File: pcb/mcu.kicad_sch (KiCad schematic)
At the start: 13 parts, among them J2 Conn_02x03_Counter_Clockwise, SW6 SW_MEC_5E, U3 STM32F042K6Tx, U4 TLV70033_SOT23-5

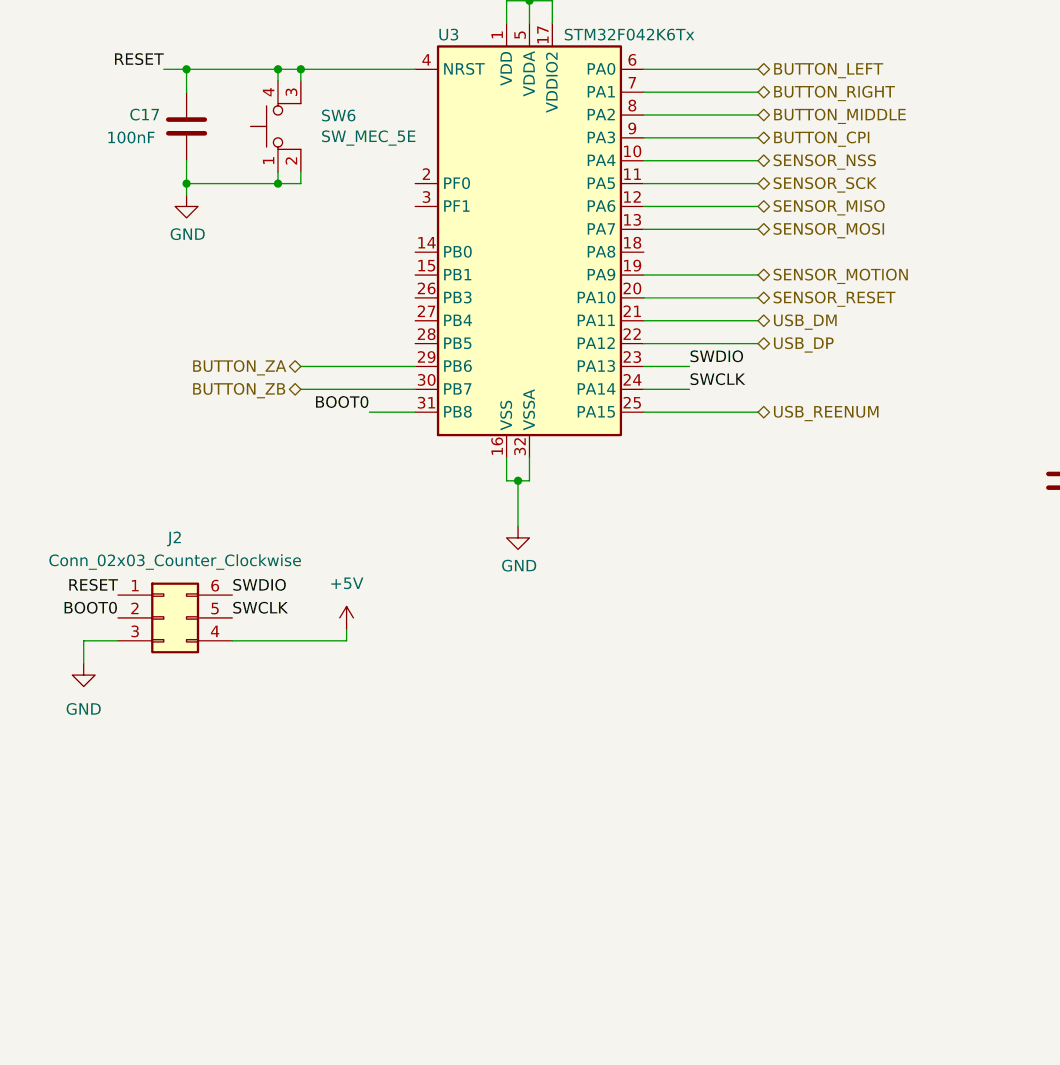
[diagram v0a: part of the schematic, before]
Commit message: - added debouncing to buttons - assigned some footprints - added expansion and inspection pin headers
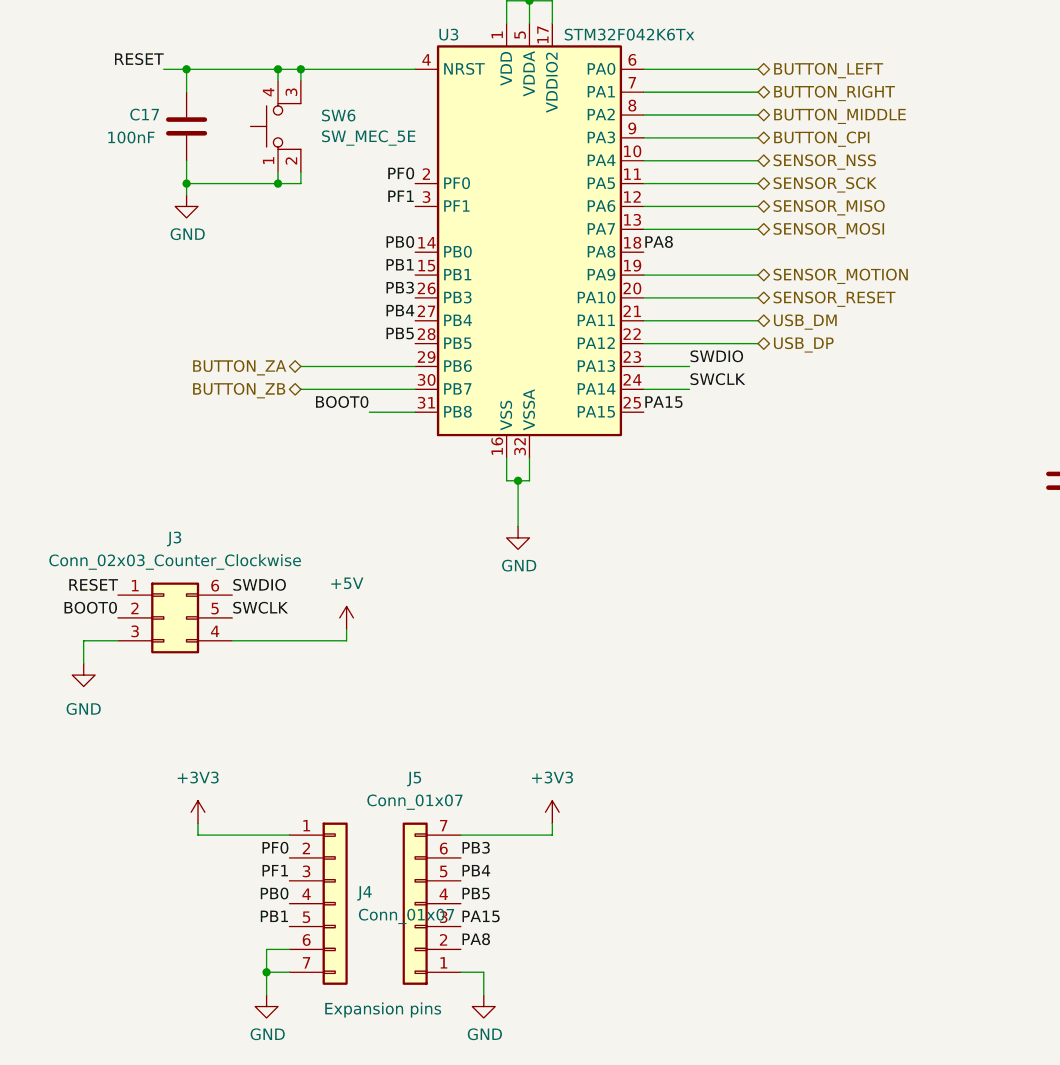
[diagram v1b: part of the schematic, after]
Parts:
- added J4, J5: Conn_01x07, Connector_PinSocket_2.54mm:PinSocket_1x07_P2.54mm_Vertical, symbol Connector_Generic:Conn_01x07
- renumbered J2 to J3
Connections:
- net +3V3: now also J4.1 (Pin_1), J5.7 (Pin_7)
- net GND: now also J4.6 (Pin_6), J4.7 (Pin_7), J5.1 (Pin_1)
- net PB0: now reaches U3.14 (PB0)
- net PB0: now also J4.4 (Pin_4)
- net PB1: now reaches U3.15 (PB1)
- net PB1: now also J4.5 (Pin_5)
- net PA8: now reaches U3.18 (PA8)
- net PA8: now also J5.2 (Pin_2)
- net PF0: now reaches U3.2 (PF0)
- net PF0: now also J4.2 (Pin_2)
- net PB3: now reaches U3.26 (PB3)
- net PB3: now also J5.6 (Pin_6)
- net PB4: now reaches U3.27 (PB4)
- net PB4: now also J5.5 (Pin_5)
- net PB5: now reaches U3.28 (PB5)
- net PB5: now also J5.4 (Pin_4)
- net PF1: now reaches U3.3 (PF1)
- net PF1: now also J4.3 (Pin_3)
- net USB_REENUM renamed PA15
- net PA15: now also J5.3 (Pin_3)
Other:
- note added: "Expansion pins"

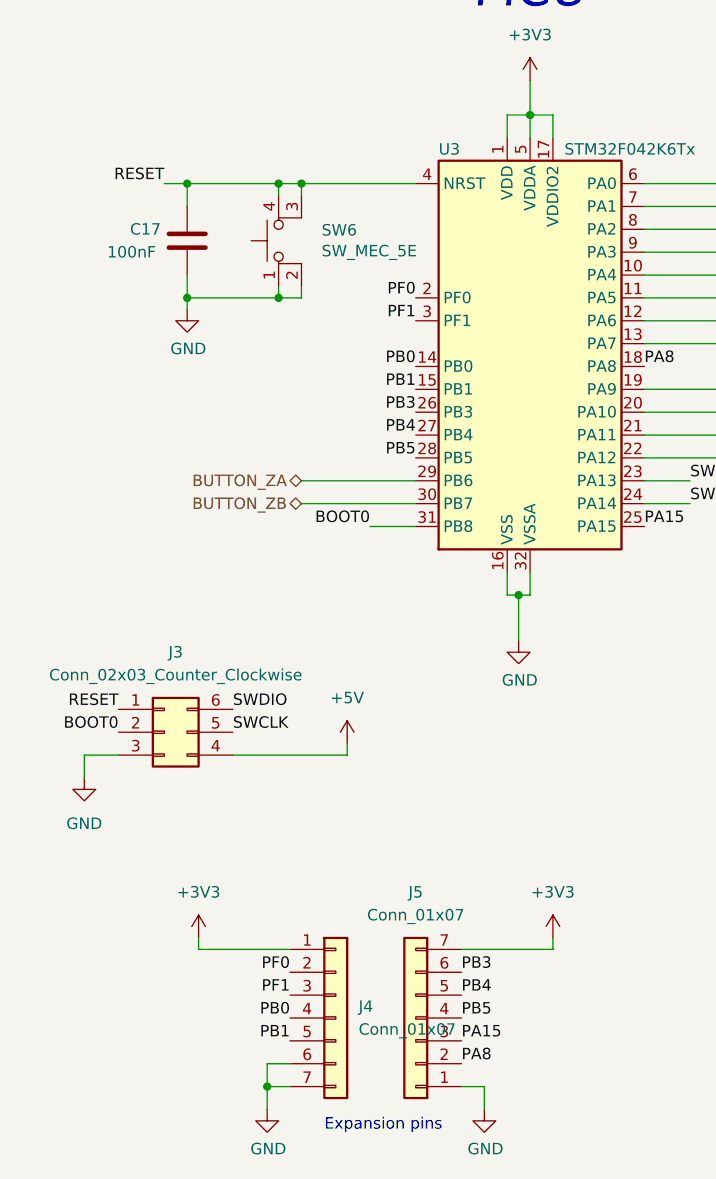
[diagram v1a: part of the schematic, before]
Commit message: - added rotary encoder debouncing - added mouse switch and encoder footprints - changed some symbols - assigned footprints
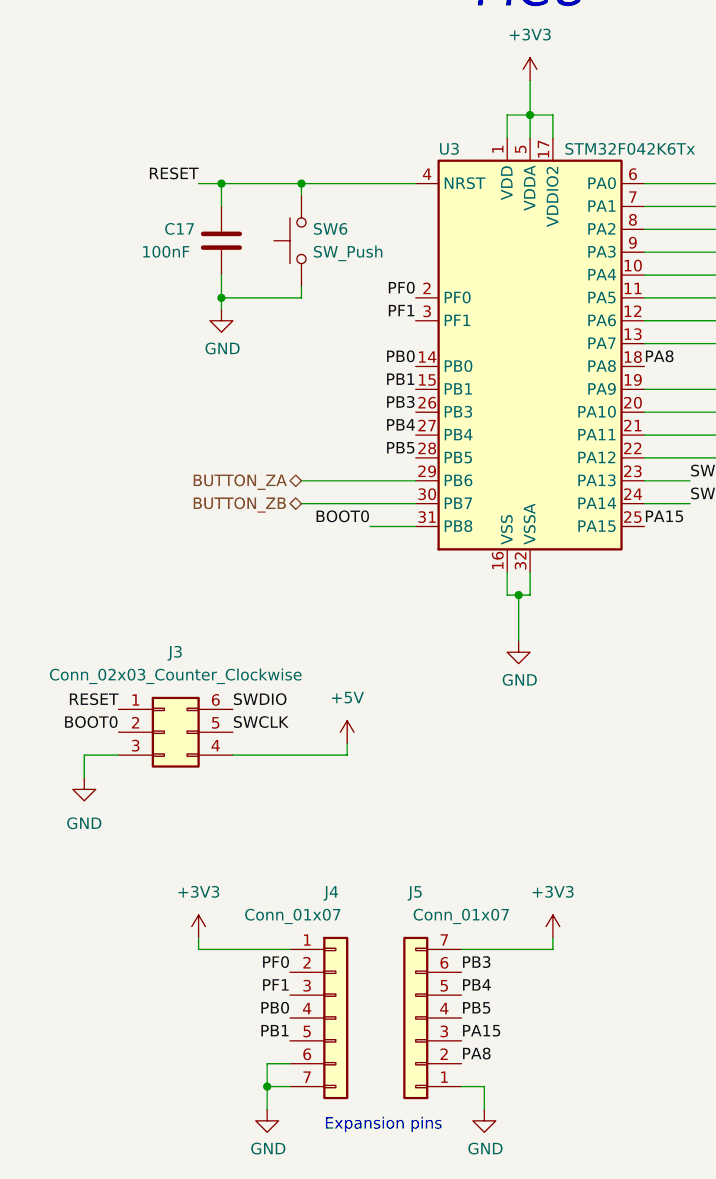
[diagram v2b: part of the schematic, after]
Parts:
- removed SW6: SW_MEC_5E, symbol Switch:SW_MEC_5E
- added SW6: SW_Push, Button_Switch_THT:SW_PUSH_6mm, symbol Switch:SW_Push
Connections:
- net GND: now also SW6.1
- net RESET: now also SW6.2
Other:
- moved on the sheet: C17
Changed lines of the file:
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@@
   (junction (at 233.68 64.77) (diameter 0) (color 0 0 0 0)
   )
-  (junction (at 92.71 76.2) (diameter 0) (color 0 0 0 0)
-  )
-  (junction (at 92.71 63.5) (diameter 0) (color 0 0 0 0)
+  (junction (at 96.52 76.2) (diameter 0) (color 0 0 0 0)
+  )
+  (junction (at 96.52 63.5) (diameter 0) (color 0 0 0 0)
   )
   (junction (at 219.71 114.3) (diameter 0) (color 0 0 0 0)
@@
   (junction (at 105.41 63.5) (diameter 0) (color 0 0 0 0)
   )
-  (junction (at 102.87 76.2) (diameter 0) (color 0 0 0 0)
-  )
   (junction (at 101.6 163.83) (diameter 0) (color 0 0 0 0)
   )
   (junction (at 208.28 64.77) (diameter 0) (color 0 0 0 0)
   )
-  (junction (at 102.87 63.5) (diameter 0) (color 0 0 0 0)
-  )
   (junction (at 219.71 104.14) (diameter 0) (color 0 0 0 0)
   )
@@
     (stroke (width 0) (type default) (color 0 0 0 0))
   )
-  (wire (pts (xy 92.71 66.04) (xy 92.71 63.5))
+  (wire (pts (xy 96.52 66.04) (xy 96.52 63.5))
     (stroke (width 0) (type default) (color 0 0 0 0))
   )
@@
     (stroke (width 0) (type default) (color 0 0 0 0))
   )
-  (wire (pts (xy 102.87 63.5) (xy 102.87 64.77))
-    (stroke (width 0) (type default) (color 0 0 0 0))
-  )
   (wire (pts (xy 214.63 114.3) (xy 219.71 114.3))
     (stroke (width 0) (type default) (color 0 0 0 0))
@@
     (stroke (width 0) (type default) (color 0 0 0 0))
   )
-  (wire (pts (xy 102.87 76.2) (xy 105.41 76.2))
-    (stroke (width 0) (type default) (color 0 0 0 0))
-  )
   (wire (pts (xy 81.28 127) (xy 81.28 129.54))
     (stroke (width 0) (type default) (color 0 0 0 0))
@@
     (stroke (width 0) (type default) (color 0 0 0 0))
   )
-  (wire (pts (xy 105.41 63.5) (xy 102.87 63.5))
-    (stroke (width 0) (type default) (color 0 0 0 0))
-  )
   (wire (pts (xy 219.71 114.3) (xy 226.06 114.3))
     (stroke (width 0) (type default) (color 0 0 0 0))
@@
     (stroke (width 0) (type default) (color 0 0 0 0))
   )
-  (wire (pts (xy 92.71 77.47) (xy 92.71 76.2))
+  (wire (pts (xy 96.52 77.47) (xy 96.52 76.2))
     (stroke (width 0) (type default) (color 0 0 0 0))
   )
@@
     (stroke (width 0) (type default) (color 0 0 0 0))
   )
-  (wire (pts (xy 90.17 63.5) (xy 92.71 63.5))
+  (wire (pts (xy 93.98 63.5) (xy 96.52 63.5))
     (stroke (width 0) (type default) (color 0 0 0 0))
   )
@@
     (stroke (width 0) (type default) (color 0 0 0 0))
   )
-  (wire (pts (xy 102.87 74.93) (xy 102.87 76.2))
-    (stroke (width 0) (type default) (color 0 0 0 0))
-  )
   (wire (pts (xy 130.81 52.07) (xy 130.81 55.88))
     (stroke (width 0) (type default) (color 0 0 0 0))
@@
     (stroke (width 0) (type default) (color 0 0 0 0))
   )
-  (wire (pts (xy 92.71 76.2) (xy 102.87 76.2))
+  (wire (pts (xy 96.52 76.2) (xy 105.41 76.2))
     (stroke (width 0) (type default) (color 0 0 0 0))
   )
@@
     (stroke (width 0) (type default) (color 0 0 0 0))
   )
-  (wire (pts (xy 92.71 63.5) (xy 102.87 63.5))
-    (stroke (width 0) (type default) (color 0 0 0 0))
-  )
-  (wire (pts (xy 92.71 73.66) (xy 92.71 76.2))
+  (wire (pts (xy 96.52 63.5) (xy 105.41 63.5))
+    (stroke (width 0) (type default) (color 0 0 0 0))
+  )
+  (wire (pts (xy 96.52 73.66) (xy 96.52 76.2))
     (stroke (width 0) (type default) (color 0 0 0 0))
   )
@@
     (effects (font (size 1.27 1.27)) (justify left bottom))
   )
-  (label "RESET" (at 90.17 63.5 180)
+  (label "RESET" (at 93.98 63.5 180)
     (effects (font (size 1.27 1.27)) (justify right bottom))
   )
@@
     (pin "1")
     (pin "2")
-  )
-  (symbol (lib_id "Switch:SW_MEC_5E") (at 105.41 69.85 90) (unit 1)
-    (in_bom yes) (on_board yes)
-    (property "Reference" "SW6" (id 0) (at 107.6452 68.6816 90)
-      (effects (font (size 1.27 1.27)) (justify right))
-    )
-    (property "Value" "SW_MEC_5E" (id 1) (at 107.6452 70.993 90)
-      (effects (font (size 1.27 1.27)) (justify right))
-    )
-    (property "Footprint" "" (id 2) (at 97.79 69.85 0)
-      (effects (font (size 1.27 1.27)) hide)
-    )
-    (property "Datasheet" "http://www.apem.com/int/index.php?controller=attachment&id_attachment=1371" (id 3) (at 97.79 69.85 0)
-      (effects (font (size 1.27 1.27)) hide)
-    )
-    (pin "1")
-    (pin "2")
-    (pin "3")
-    (pin "4")
   )
   (symbol (lib_id "power:+3V3") (at 130.81 52.07 0) (unit 1)
@@
     (pin "1")
   )
-  (symbol (lib_id "Device:C") (at 92.71 69.85 0) (unit 1)
-    (in_bom yes) (on_board yes)
-    (property "Reference" "C17" (id 0) (at 86.36 68.58 0)
-      (effects (font (size 1.27 1.27)) (justify left))
-    )
-    (property "Value" "100nF" (id 1) (at 83.82 71.12 0)
-      (effects (font (size 1.27 1.27)) (justify left))
-    )
-    (property "Footprint" "Capacitor_SMD:C_0603_1608Metric" (id 2) (at 93.6752 73.66 0)
-      (effects (font (size 1.27 1.27)) hide)
-    )
-    (property "Datasheet" "~" (id 3) (at 92.71 69.85 0)
+  (symbol (lib_id "Device:C") (at 96.52 69.85 0) (unit 1)
+    (in_bom yes) (on_board yes)
+    (property "Reference" "C17" (id 0) (at 90.17 68.58 0)
+      (effects (font (size 1.27 1.27)) (justify left))
+    )
+    (property "Value" "100nF" (id 1) (at 87.63 71.12 0)
+      (effects (font (size 1.27 1.27)) (justify left))
+    )
+    (property "Footprint" "Capacitor_SMD:C_0603_1608Metric" (id 2) (at 97.4852 73.66 0)
+      (effects (font (size 1.27 1.27)) hide)
+    )
+    (property "Datasheet" "~" (id 3) (at 96.52 69.85 0)
       (effects (font (size 1.27 1.27)) hide)
     )
@@
     (pin "1")
   )
-  (symbol (lib_id "power:GND") (at 92.71 77.47 0) (unit 1)
-    (in_bom yes) (on_board yes)
-    (property "Reference" "#PWR033" (id 0) (at 92.71 83.82 0)
-      (effects (font (size 1.27 1.27)) hide)
-    )
-    (property "Value" "GND" (id 1) (at 92.837 81.8642 0))
-    (property "Footprint" "" (id 2) (at 92.71 77.47 0)
-      (effects (font (size 1.27 1.27)) hide)
-    )
-    (property "Datasheet" "" (id 3) (at 92.71 77.47 0)
+  (symbol (lib_id "Switch:SW_Push") (at 105.41 69.85 90) (unit 1)
+    (in_bom yes) (on_board yes) (fields_autoplaced)
+    (property "Reference" "SW6" (id 0) (at 106.68 68.5799 90)
+      (effects (font (size 1.27 1.27)) (justify right))
+    )
+    (property "Value" "SW_Push" (id 1) (at 106.68 71.1199 90)
+      (effects (font (size 1.27 1.27)) (justify right))
+    )
+    (property "Footprint" "Button_Switch_THT:SW_PUSH_6mm" (id 2) (at 100.33 69.85 0)
+      (effects (font (size 1.27 1.27)) hide)
+    )
+    (property "Datasheet" "~" (id 3) (at 100.33 69.85 0)
+      (effects (font (size 1.27 1.27)) hide)
+    )
+    (pin "1")
+    (pin "2")
+  )
+  (symbol (lib_id "power:GND") (at 96.52 77.47 0) (unit 1)
+    (in_bom yes) (on_board yes)
+    (property "Reference" "#PWR033" (id 0) (at 96.52 83.82 0)
+      (effects (font (size 1.27 1.27)) hide)
+    )
+    (property "Value" "GND" (id 1) (at 96.647 81.8642 0))
+    (property "Footprint" "" (id 2) (at 96.52 77.47 0)
+      (effects (font (size 1.27 1.27)) hide)
+    )
+    (property "Datasheet" "" (id 3) (at 96.52 77.47 0)
       (effects (font (size 1.27 1.27)) hide)
     )
@@
   )
   (symbol (lib_id "Connector_Generic:Conn_01x07") (at 118.11 156.21 180) (unit 1)
-    (in_bom yes) (on_board yes) (fields_autoplaced)
+    (in_bom yes) (on_board yes)
     (property "Reference" "J5" (id 0) (at 118.11 142.24 0))
-    (property "Value" "Conn_01x07" (id 1) (at 118.11 144.78 0))
+    (property "Value" "Conn_01x07" (id 1) (at 123.19 144.78 0))
     (property "Footprint" "Connector_PinSocket_2.54mm:PinSocket_1x07_P2.54mm_Vertical" (id 2) (at 118.11 156.21 0)
       (effects (font (size 1.27 1.27)) hide)
@@
   )
   (symbol (lib_id "Connector_Generic:Conn_01x07") (at 109.22 156.21 0) (unit 1)
-    (in_bom yes) (on_board yes) (fields_autoplaced)
-    (property "Reference" "J4" (id 0) (at 111.76 154.9399 0)
-      (effects (font (size 1.27 1.27)) (justify left))
-    )
-    (property "Value" "Conn_01x07" (id 1) (at 111.76 157.4799 0)
-      (effects (font (size 1.27 1.27)) (justify left))
-    )
+    (in_bom yes) (on_board yes)
+    (property "Reference" "J4" (id 0) (at 107.95 142.24 0)
+      (effects (font (size 1.27 1.27)) (justify left))
+    )
+    (property "Value" "Conn_01x07" (id 1) (at 99.06 144.78 0)
+      (effects (font (size 1.27 1.27)) (justify left))
+    )
